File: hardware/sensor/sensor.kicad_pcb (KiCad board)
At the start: 2 copper layers, 83.8 x 68.6 mm, 10 parts

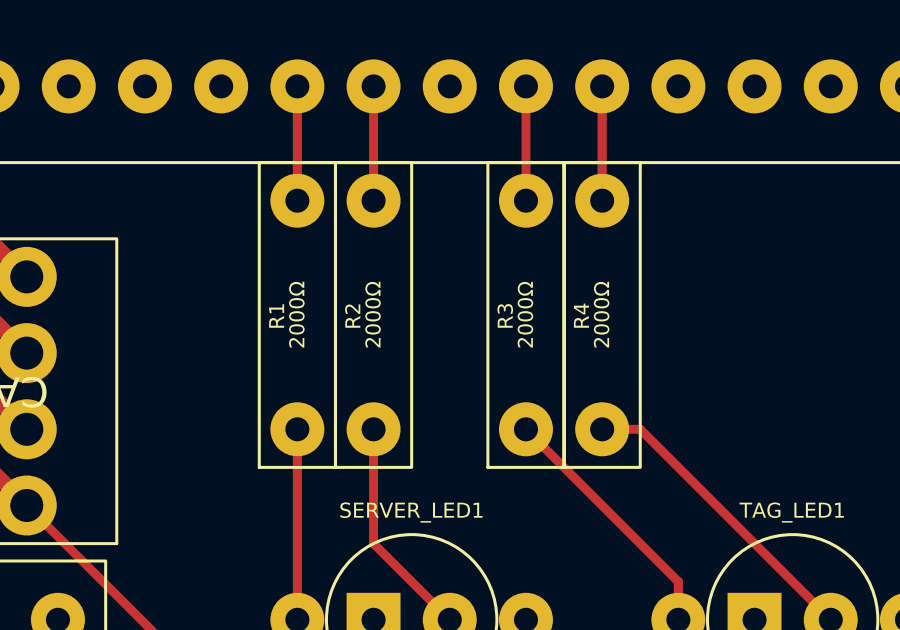
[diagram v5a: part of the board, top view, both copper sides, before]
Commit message: hardware: Increase the LED resistor from 2000Ω to 10KΩ.
To reduce the power consumption.
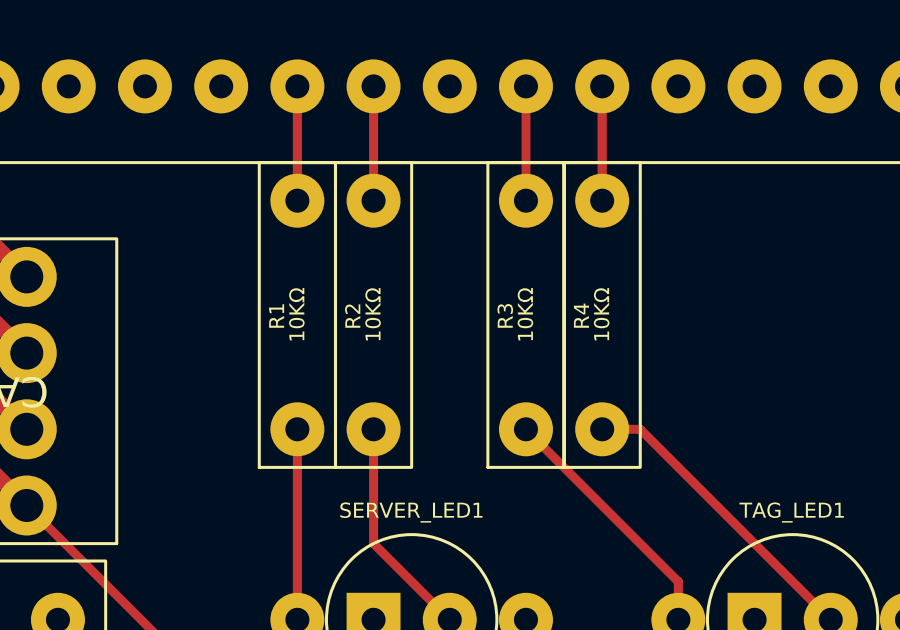
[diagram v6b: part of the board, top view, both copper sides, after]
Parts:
- R1, R2, R3, R4: value 2000Ω -> 10KΩ
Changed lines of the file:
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@@
 			)
 		)
-		(property "Value" "2000Ω"
+		(property "Value" "10KΩ"
 			(at 3.81 0 90)
 			(unlocked yes)
@@
 			)
 		)
-		(property "Value" "2000Ω"
+		(property "Value" "10KΩ"
 			(at 3.81 0 90)
 			(unlocked yes)
@@
 			)
 		)
-		(property "Value" "2000Ω"
+		(property "Value" "10KΩ"
 			(at 3.81 0 90)
 			(unlocked yes)
@@
 			)
 		)
-		(property "Value" "2000Ω"
+		(property "Value" "10KΩ"
 			(at 3.81 0 90)
 			(unlocked yes)

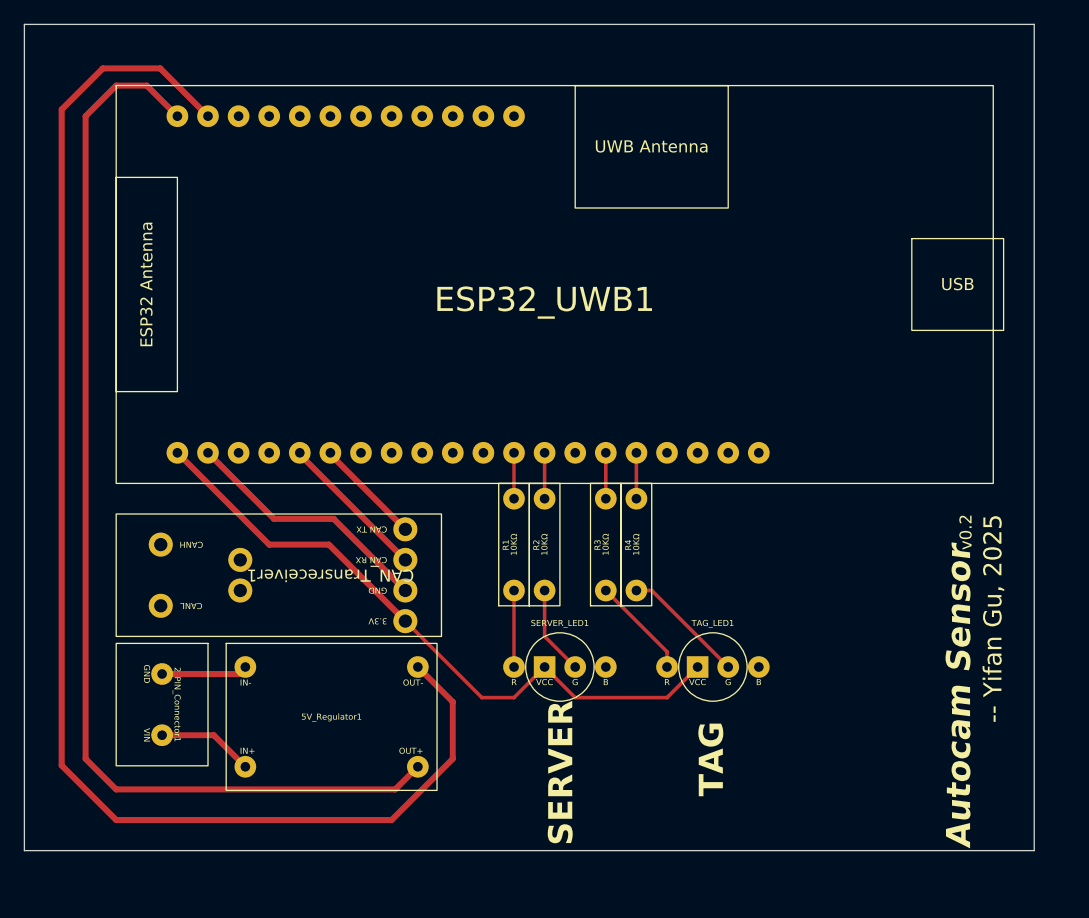
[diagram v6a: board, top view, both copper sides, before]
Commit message: hardware: Reroute the wires to fix unavailable PINs.
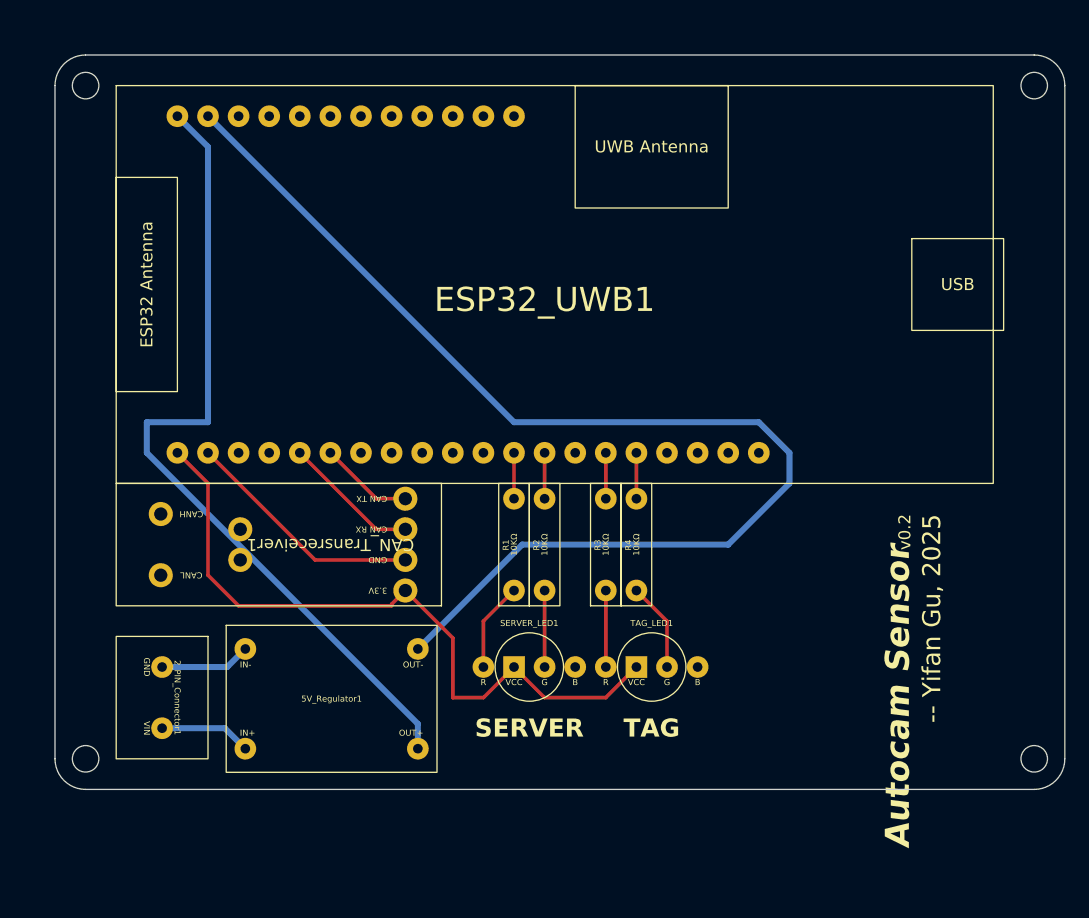
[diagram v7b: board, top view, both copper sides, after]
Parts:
- added REF**: MountingHole_2.2mm_M2, MountingHole:MountingHole_2.2mm_M2, F.Cu at (124.5, 124.5)
- added REF**: MountingHole_2.2mm_M2, MountingHole:MountingHole_2.2mm_M2, F.Cu at (124.5, 68.6)
- added REF**: MountingHole_2.2mm_M2, MountingHole:MountingHole_2.2mm_M2, F.Cu at (203.2, 124.5)
- added REF**: MountingHole_2.2mm_M2, MountingHole:MountingHole_2.2mm_M2, F.Cu at (203.2, 68.6)
- moved TAG_LED1 5.08 mm to (171.4, 116.8)
- moved SERVER_LED1 2.54 mm to (161.3, 116.8)
- moved CAN_Transreceiver1 2.54 mm to (127.0, 101.6)
- moved 5V_Regulator1 1.50 mm to (136.1, 113.4)
- moved 2_PIN_Connector1 0.58 mm to (127.0, 114.3)
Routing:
- net Net-(5V_Regulator1-OUT+): track 92.5 -> 68.0 mm
- net Net-(5V_Regulator1-OUT-): track 114.9 -> 98.9 mm
- net Net-(CAN_Transreceiver1-3.3V): track 54.8 -> 58.2 mm
- net Net-(TAG_LED1-G): track 10.3 -> 7.40 mm
- net Net-(TAG_LED1-R): track 8.45 -> 6.35 mm
- net Net-(SERVER_LED1-R): track 6.35 -> 7.40 mm
- net Net-(SERVER_LED1-G): track 7.40 -> 6.35 mm
- net Net-(CAN_Transreceiver1-GND): track 21.1 -> 20.1 mm
- net Net-(CAN_Transreceiver1-CAN_RX): track 12.5 -> 11.5 mm
- net Net-(CAN_Transreceiver1-CAN_TX): track 8.93 -> 7.93 mm
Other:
- board size 83.8 x 68.6 mm -> 83.8 x 61 mm

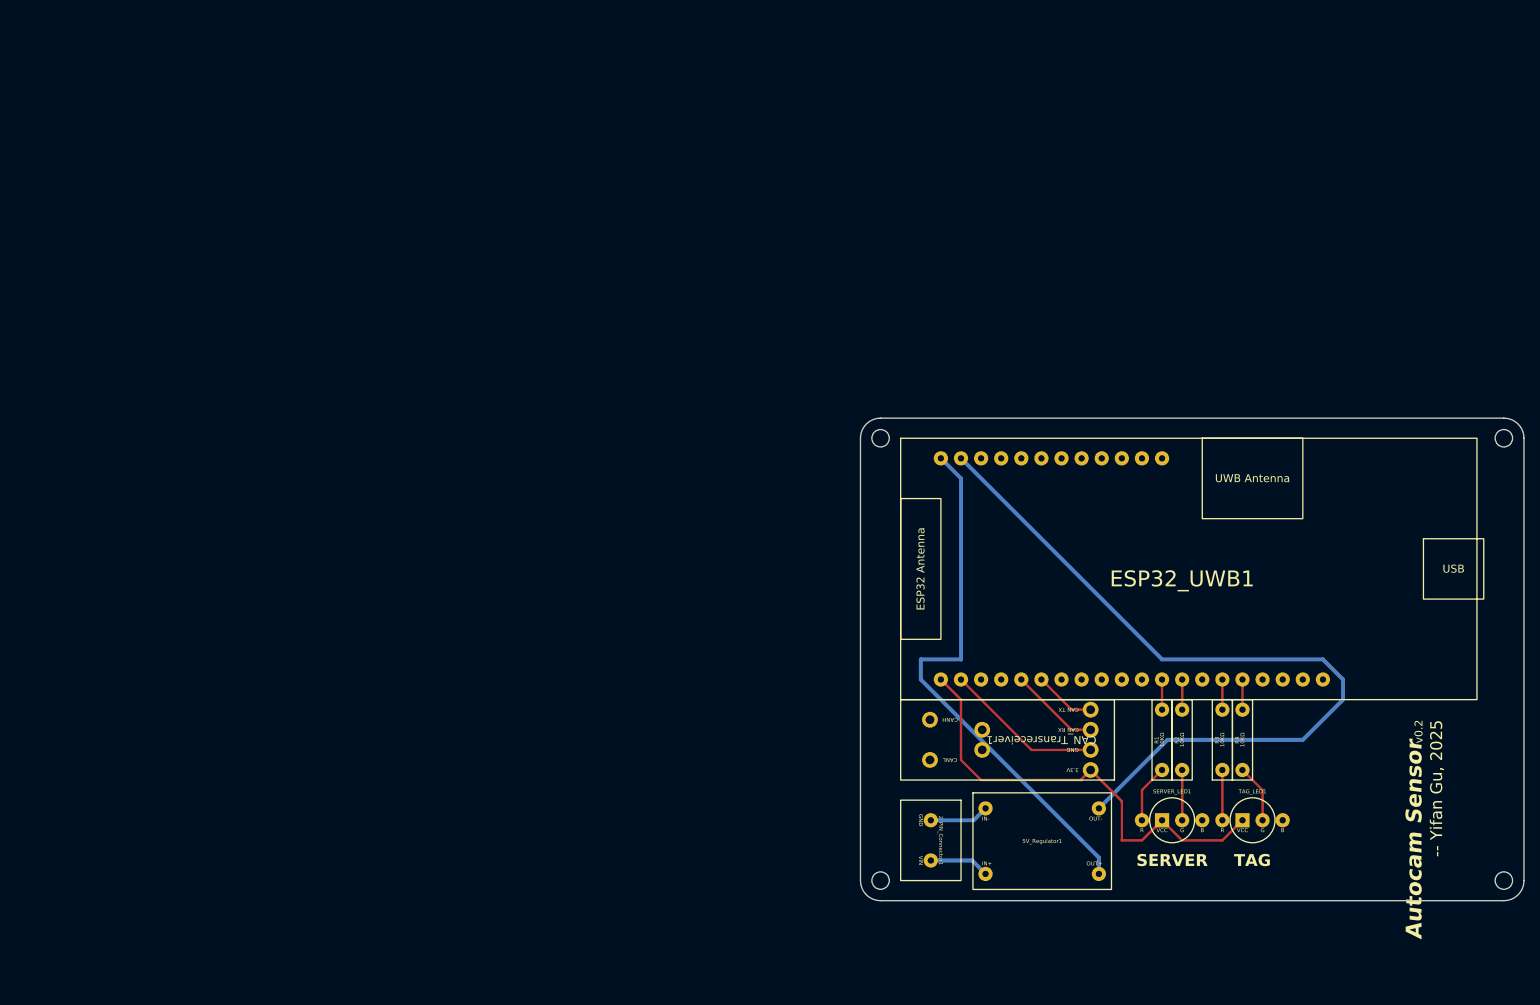
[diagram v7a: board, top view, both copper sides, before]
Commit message: hardware: Move the PCB to near the coordinate origin.
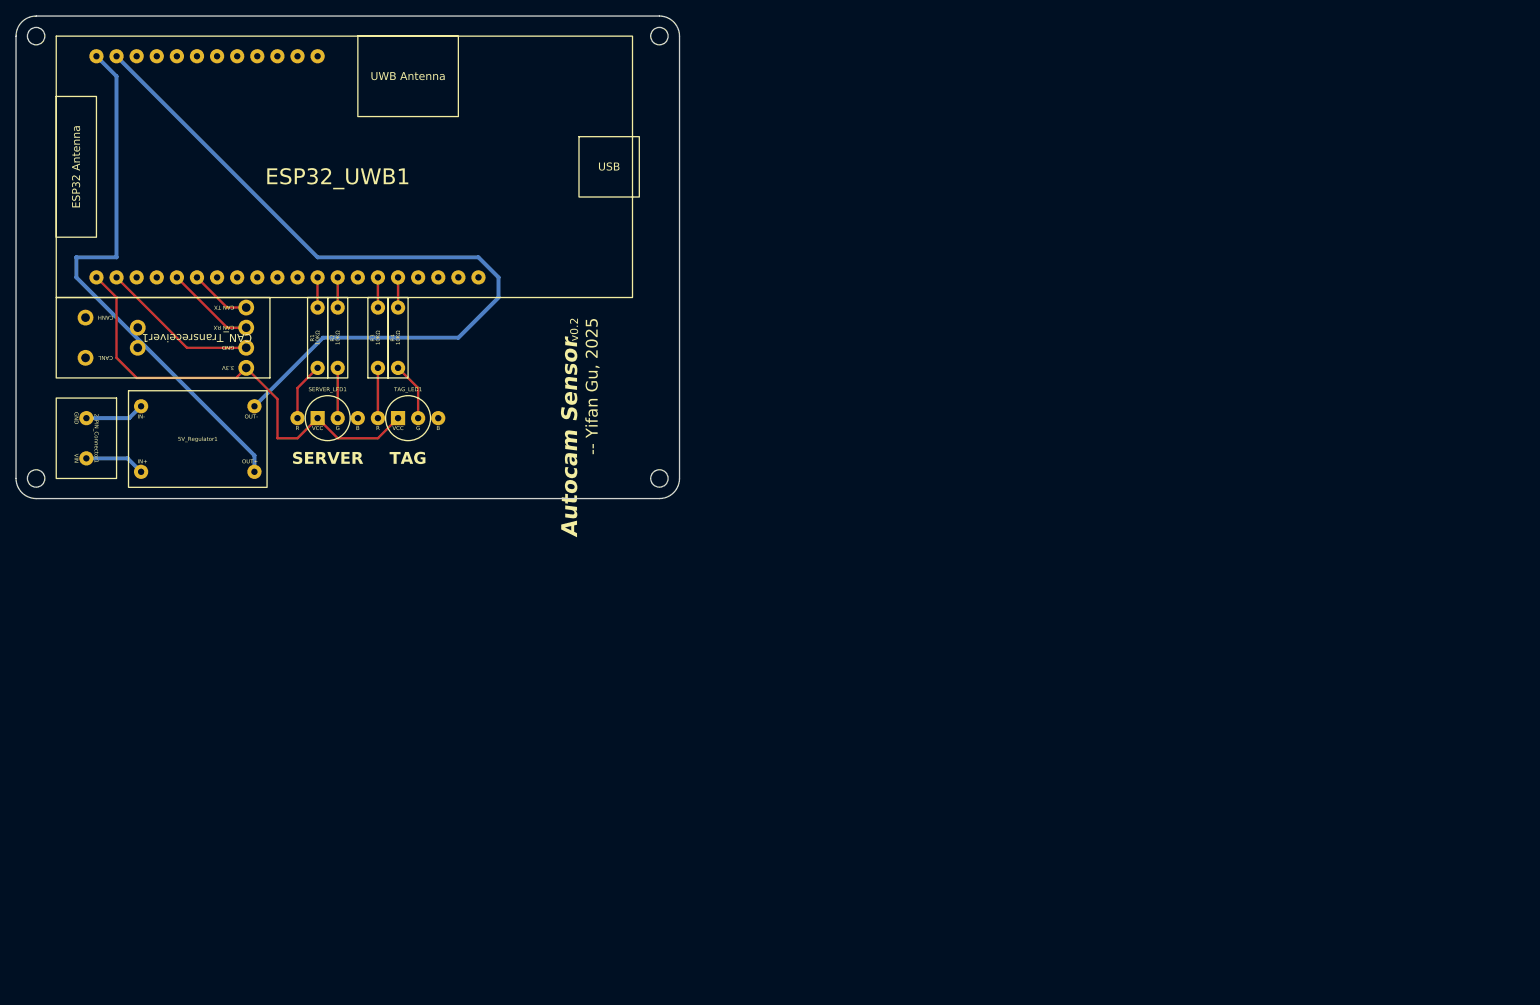
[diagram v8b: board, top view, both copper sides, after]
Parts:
- moved 2_PIN_Connector1 118.2 mm to (20.3, 63.5)
- moved CAN_Transreceiver1 118.2 mm to (20.3, 50.8)
- moved ESP32_UWB1 118.2 mm to (20.3, 17.8)
- moved R1 118.2 mm to (53.3, 59.7)
- moved R2 118.2 mm to (55.9, 59.7)
- moved R4 118.2 mm to (63.5, 59.7)
- moved 5V_Regulator1 118.2 mm to (29.4, 62.6)
- moved REF** 118.2 mm to (17.8, 73.7)
- moved REF** 118.2 mm to (17.8, 17.8)
- moved REF** 118.2 mm to (96.5, 73.7)
- moved REF** 118.2 mm to (96.5, 17.8)
- moved SERVER_LED1 118.2 mm to (54.6, 66.0)
- moved TAG_LED1 118.2 mm to (64.8, 66.0)
- moved R3 118.2 mm to (61.0, 59.7)
